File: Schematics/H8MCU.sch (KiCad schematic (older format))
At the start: 5 parts

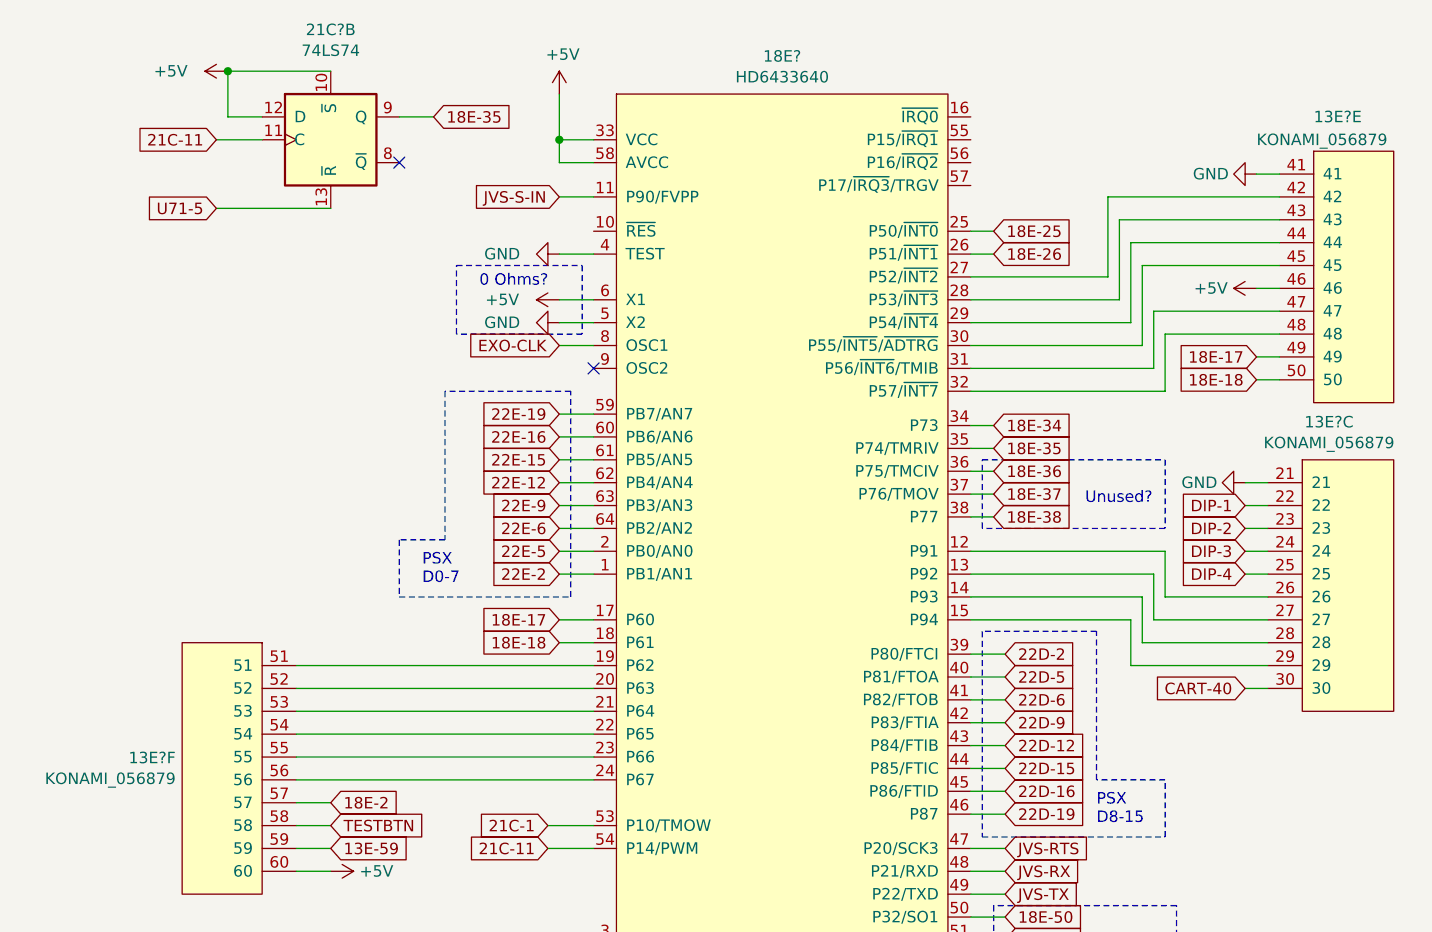
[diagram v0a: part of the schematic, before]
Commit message: Added GE675-PWB(A)
IO Board for Fisherman's Bait 3
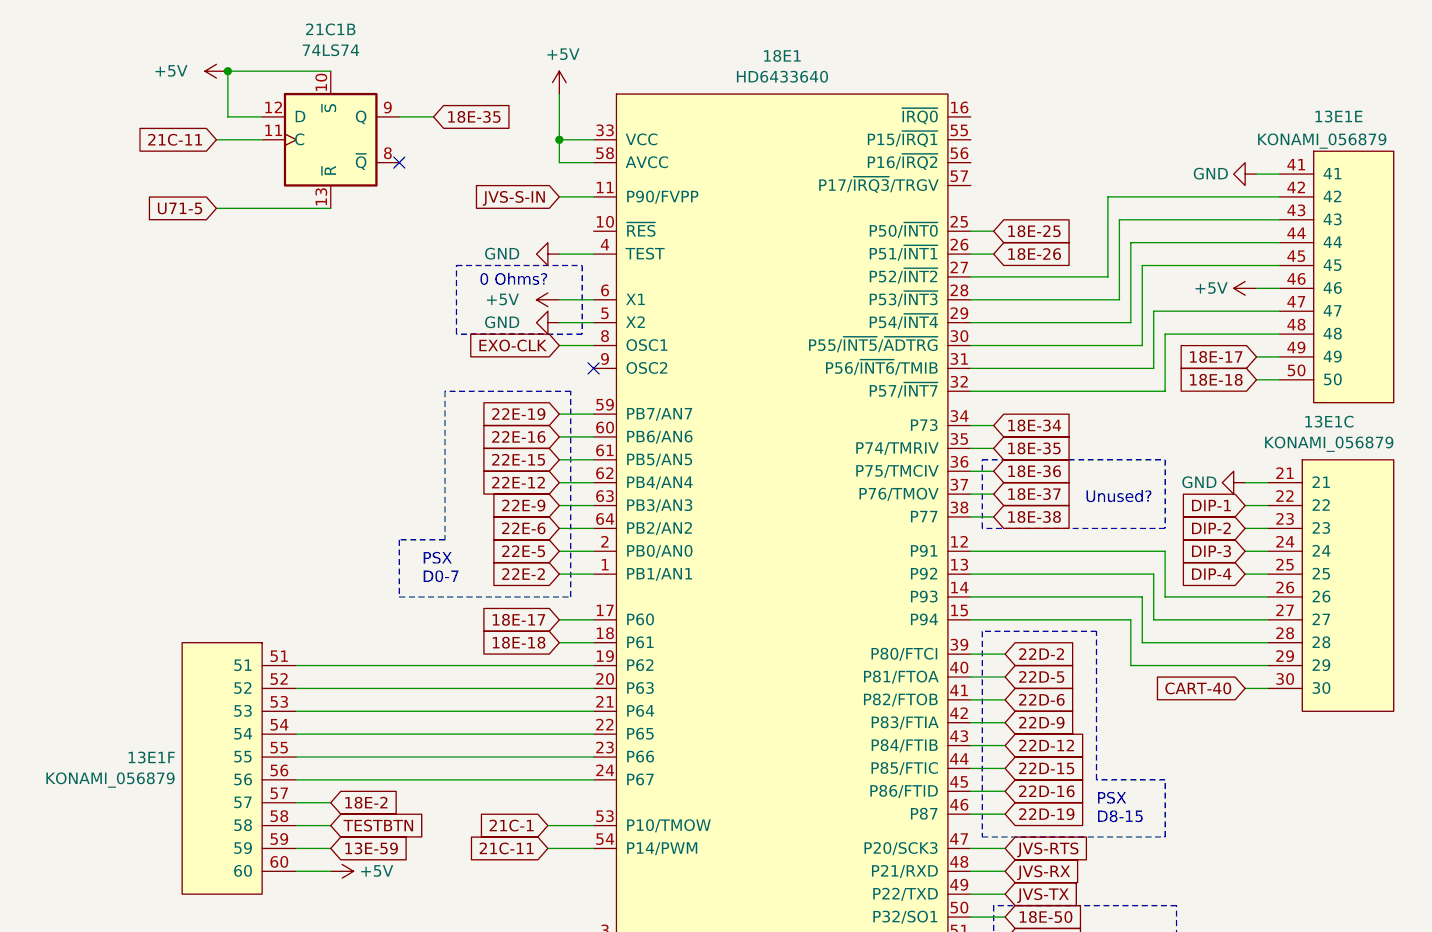
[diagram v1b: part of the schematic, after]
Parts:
- gave numbers to parts that had none: 3
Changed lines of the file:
@@
 $EndDescr
 $Comp
-L MCU_Hitachi:HD6433640 18E?
+L MCU_Hitachi:HD6433640 18E1
 U 1 1 64ADE90A
 P 5050 4050
-F 0 "18E?" H 5025 6315 50  0000 C CNN
+F 0 "18E1" H 5025 6315 50  0000 C CNN
 F 1 "HD6433640" H 5025 6224 50  0000 C CNN
 F 2 "Package_QFP:TQFP-64_10x10mm_P0.5mm" H 5000 2100 50  0001 C CNN
@@
 $EndComp
 $Comp
-L power:+5V #PWR?
+L power:+5V #PWR0158
 U 1 1 64ADE910
 P 4050 1950
-F 0 "#PWR?" H 4050 1800 50  0001 C CNN
+F 0 "#PWR0158" H 4050 1800 50  0001 C CNN
 F 1 "+5V" H 4065 2123 50  0000 C CNN
 F 2 "" H 4050 1950 50  0001 C CNN
@@
 Connection ~ 4050 2150
 $Comp
-L Arcade:KONAMI_056879 13E?
+L Arcade:KONAMI_056879 13E1
 U 6 1 64ADE91B
 P 2550 5550
-F 0 "13E?" H 2728 6246 50  0000 L CNN
+F 0 "13E1" H 2728 6246 50  0000 L CNN
 F 1 "KONAMI_056879" H 2728 6155 50  0000 L CNN
 F 2 "Package_QFP:TQFP-120_14x14mm_P0.4mm" H 2550 5550 50  0001 C CNN
@@
 DIP-1
 $Comp
-L Arcade:KONAMI_056879 13E?
+L Arcade:KONAMI_056879 13E1
 U 3 1 64ADE926
 P 7500 4750
-F 0 "13E?" H 7417 6115 50  0000 C CNN
+F 0 "13E1" H 7417 6115 50  0000 C CNN
 F 1 "KONAMI_056879" H 7417 6024 50  0000 C CNN
 F 2 "Package_QFP:TQFP-120_14x14mm_P0.4mm" H 7500 4750 50  0001 C CNN
@@
 $EndComp
 $Comp
-L power:GND #PWR?
+L power:GND #PWR0159
 U 1 1 64ADE92C
 P 7050 3650
-F 0 "#PWR?" H 7050 3400 50  0001 C CNN
+F 0 "#PWR0159" H 7050 3400 50  0001 C CNN
 F 1 "GND" V 7050 3450 50  0000 C CNN
 F 2 "" H 7050 3650 50  0001 C CNN
@@
 	7050 4550 7150 4550
 $Comp
-L Arcade:KONAMI_056879 13E?
+L Arcade:KONAMI_056879 13E1
 U 5 1 64ADE938
 P 7550 3400
-F 0 "13E?" H 7350 4750 50  0000 L CNN
+F 0 "13E1" H 7350 4750 50  0000 L CNN
 F 1 "KONAMI_056879" H 7100 4650 50  0000 L CNN
 F 2 "Package_QFP:TQFP-120_14x14mm_P0.4mm" H 7550 3400 50  0001 C CNN
@@
 	7200 3000 6700 3000
 $Comp
-L power:+5V #PWR?
+L power:+5V #PWR0160
 U 1 1 64ADE940
 P 7100 2800
-F 0 "#PWR?" H 7100 2650 50  0001 C CNN
+F 0 "#PWR0160" H 7100 2650 50  0001 C CNN
 F 1 "+5V" V 7100 3000 50  0000 C CNN
 F 2 "" H 7100 2800 50  0001 C CNN
@@
 	7200 3100 7100 3100
 $Comp
-L power:GND #PWR?
+L power:GND #PWR0161
 U 1 1 64ADE94B
 P 7100 2300
-F 0 "#PWR?" H 7100 2050 50  0001 C CNN
+F 0 "#PWR0161" H 7100 2050 50  0001 C CNN
 F 1 "GND" V 7100 2100 50  0000 C CNN
 F 2 "" H 7100 2300 50  0001 C CNN
@@
 TESTBTN
 $Comp
-L power:+5V #PWR?
+L power:+5V #PWR0162
 U 1 1 64ADE95A
 P 3050 5350
-F 0 "#PWR?" H 3050 5200 50  0001 C CNN
+F 0 "#PWR0162" H 3050 5200 50  0001 C CNN
 F 1 "+5V" V 3050 5550 50  0000 C CNN
 F 2 "" H 3050 5350 50  0001 C CNN
@@
 	4100 5750 4200 5750
 $Comp
-L power:GND #PWR?
+L power:GND #PWR0163
 U 1 1 64ADE96B
 P 4100 5850
-F 0 "#PWR?" H 4100 5600 50  0001 C CNN
+F 0 "#PWR0163" H 4100 5600 50  0001 C CNN
 F 1 "GND" H 4105 5677 50  0000 C CNN
 F 2 "" H 4100 5850 50  0001 C CNN
@@
 Connection ~ 4100 5750
 $Comp
-L power:+5V #PWR?
+L power:+5V #PWR0164
 U 1 1 64ADE974
 P 4050 2850
-F 0 "#PWR?" H 4050 2700 50  0001 C CNN
+F 0 "#PWR0164" H 4050 2700 50  0001 C CNN
 F 1 "+5V" V 4050 3100 50  0000 C CNN
 F 2 "" H 4050 2850 50  0001 C CNN
@@
 	4050 2850 4200 2850
 $Comp
-L power:GND #PWR?
+L power:GND #PWR0165
 U 1 1 64ADE97B
 P 4050 2950
-F 0 "#PWR?" H 4050 2700 50  0001 C CNN
+F 0 "#PWR0165" H 4050 2700 50  0001 C CNN
 F 1 "GND" V 4050 2700 50  0000 C CNN
 F 2 "" H 4050 2950 50  0001 C CNN
@@
 0 Ohms?
 $Comp
-L power:GND #PWR?
+L power:GND #PWR0166
 U 1 1 64ADE987
 P 4050 2650
-F 0 "#PWR?" H 4050 2400 50  0001 C CNN
+F 0 "#PWR0166" H 4050 2400 50  0001 C CNN
 F 1 "GND" V 4050 2400 50  0000 C CNN
 F 2 "" H 4050 2650 50  0001 C CNN
@@
 	5850 3400 5950 3400
 $Comp
-L 74xx:74LS74 21C?
+L 74xx:74LS74 21C1
 U 2 1 64ADEA00
 P 3050 2150
-F 0 "21C?" H 3050 2631 50  0000 C CNN
+F 0 "21C1" H 3050 2631 50  0000 C CNN
 F 1 "74LS74" H 3050 2540 50  0000 C CNN
 F 2 "Package_SO:SO-14_3.9x8.65mm_P1.27mm" H 3050 2150 50  0001 C CNN
@@
 $EndComp
 $Comp
-L power:+5V #PWR?
+L power:+5V #PWR0167
 U 1 1 64ADEA06
 P 2600 1850
-F 0 "#PWR?" H 2600 1700 50  0001 C CNN
+F 0 "#PWR0167" H 2600 1700 50  0001 C CNN
 F 1 "+5V" V 2600 2100 50  0000 C CNN
 F 2 "" H 2600 1850 50  0001 C CNN

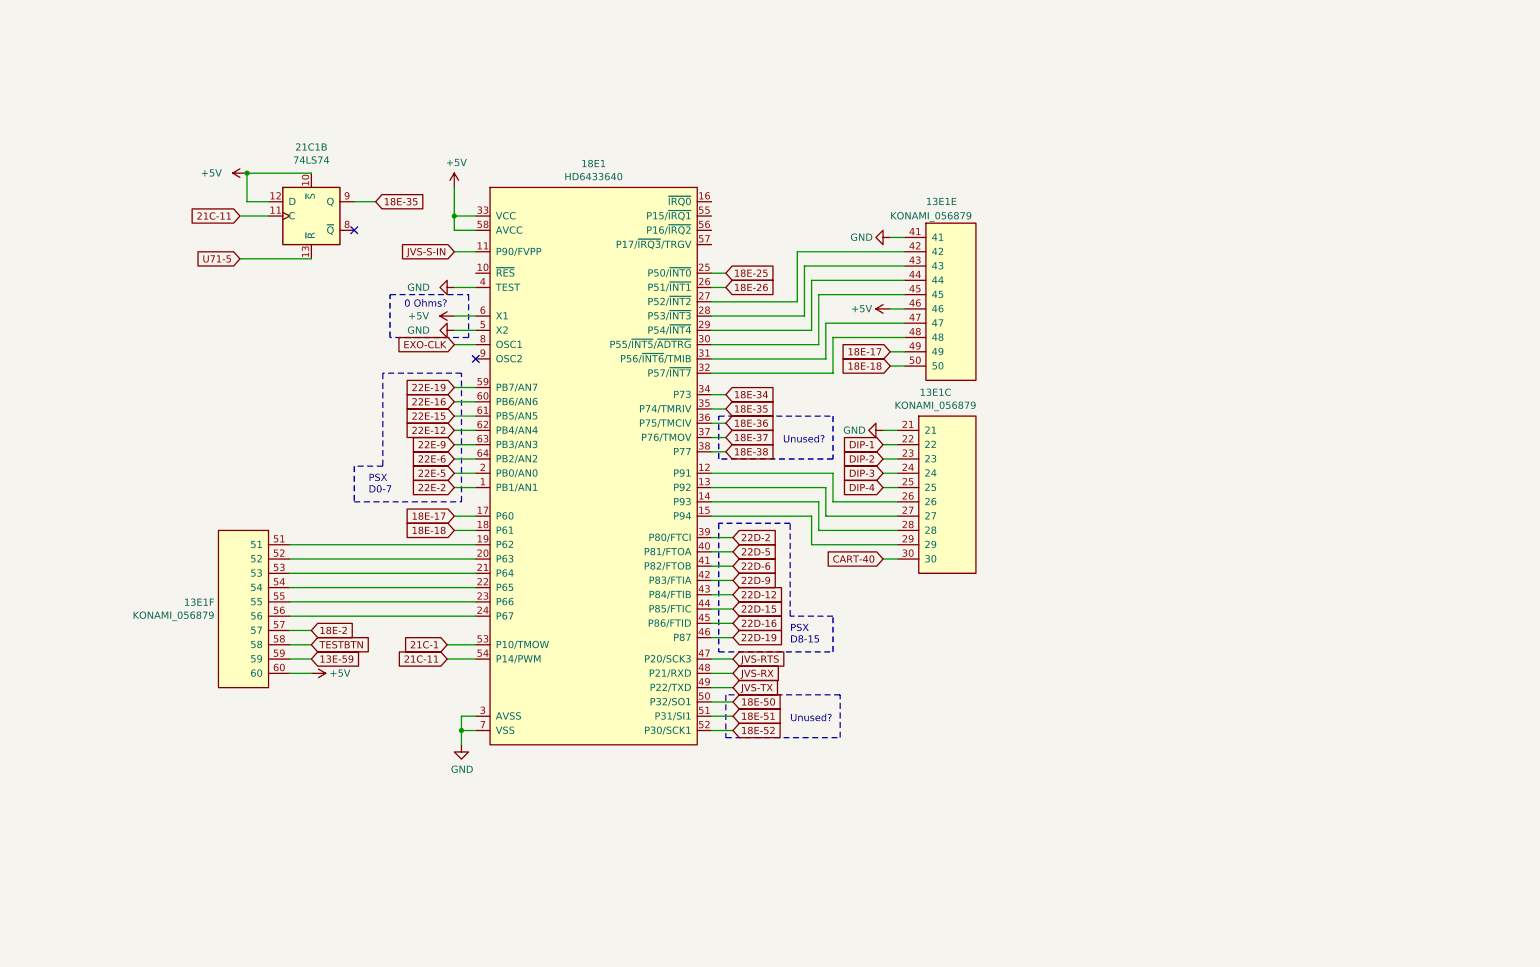
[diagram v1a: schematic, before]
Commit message: Updated Schematics
PCMCIA is pinned out
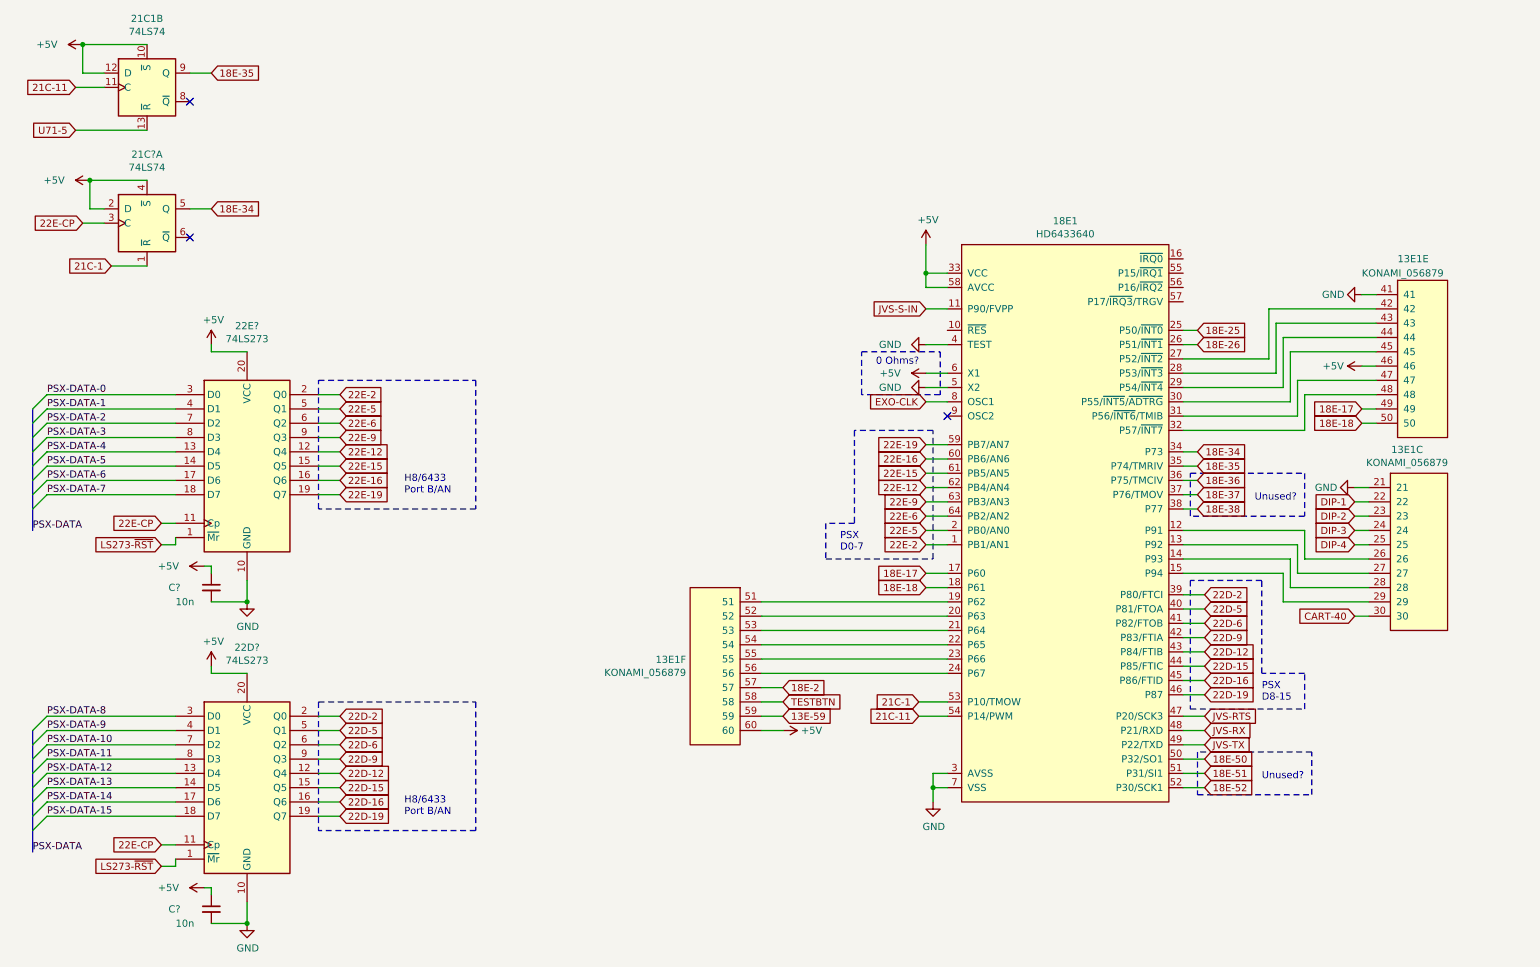
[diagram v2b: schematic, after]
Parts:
- added 21C?: 74LS74, Package_SO:SO-14_3.9x8.65mm_P1.27mm, symbol 74xx:74LS74
- added 22D?, 22E?: 74LS273, Package_SO:SO-20_5.3x12.6mm_P1.27mm, symbol 74xx:74LS273
- added C? (x2): 10n, symbol Device:C_Small
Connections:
- net +5V: now also 21C?.2 (D), 21C?.4 (~S), 22D?.20 (VCC), 22E?.20 (VCC), C?.1, C?.1
- net 18E-34: now also 21C?.5 (Q)
- net 21C-1: now also 21C?.1 (~R)
- net 22D-12: now also 22D?.12 (Q4)
- net 22D-15: now also 22D?.15 (Q5)
- net 22D-16: now also 22D?.16 (Q6)
- net 22D-19: now also 22D?.19 (Q7)
- net 22D-2: now also 22D?.2 (Q0)
- net 22D-5: now also 22D?.5 (Q1)
- net 22D-6: now also 22D?.6 (Q2)
- net 22D-9: now also 22D?.9 (Q3)
- net 22E-12: now also 22E?.12 (Q4)
- net 22E-15: now also 22E?.15 (Q5)
- net 22E-16: now also 22E?.16 (Q6)
- net 22E-19: now also 22E?.19 (Q7)
- net 22E-2: now also 22E?.2 (Q0)
- net 22E-5: now also 22E?.5 (Q1)
- net 22E-6: now also 22E?.6 (Q2)
- net 22E-9: now also 22E?.9 (Q3)
- net GND: now also 22D?.10 (GND), 22E?.10 (GND), C?.2, C?.2
- new net 22E-CP: 21C?.3 (C), 22D?.11 (Cp), 22E?.11 (Cp)
- new net LS273-~RST: 22D?.1 (~Mr), 22E?.1 (~Mr)
- new net PSX-DATA-0: 22E?.3 (D0)
- new net PSX-DATA-1: 22E?.4 (D1)
- new net PSX-DATA-10: 22D?.7 (D2)
- new net PSX-DATA-11: 22D?.8 (D3)
- new net PSX-DATA-12: 22D?.13 (D4)
- new net PSX-DATA-13: 22D?.14 (D5)
- new net PSX-DATA-14: 22D?.17 (D6)
- new net PSX-DATA-15: 22D?.18 (D7)
- new net PSX-DATA-2: 22E?.7 (D2)
- new net PSX-DATA-3: 22E?.8 (D3)
- new net PSX-DATA-4: 22E?.13 (D4)
- new net PSX-DATA-5: 22E?.14 (D5)
- new net PSX-DATA-6: 22E?.17 (D6)
- new net PSX-DATA-7: 22E?.18 (D7)
- new net PSX-DATA-8: 22D?.3 (D0)
- new net PSX-DATA-9: 22D?.4 (D1)
- no-connect marks 2 -> 3
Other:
- note added: "H8/6433\nPort B/AN"
- moved on the sheet: 13E1C, 13E1E, 13E1F, 18E1, 21C1B

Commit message: Fixed bugs
IDE Retrace, PCMCIA checked
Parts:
- removed 22D?, 22E?: 74LS273, Package_SO:SO-20_5.3x12.6mm_P1.27mm, symbol 74xx:74LS273
- removed C? (x2): 10n, symbol Device:C_Small
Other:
- note removed: "H8/6433\nPort B/AN"
